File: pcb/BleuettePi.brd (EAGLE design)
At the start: 85 x 56 mm, 104 parts, among them IC1 PIC18F452, IC2 DS1339, IC3 MAX4173FESA+, IC5 MCP23017SS, IC6 LM386M-1, IC7 GY-27, Q1 10Mhz

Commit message: First Python code
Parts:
- removed D3: 5v1, diode:SOT23
- added D1: 5v1, diode:SOT23
- added D2: 3V3, diode:SOT23
- C1, C2: value (none) -> 470uf
- C12, C16, C6: value (none) -> 100nf
- C13: value (none) -> 4.7uf; device rcl:PANASONIC_A -> rcl:CT3528
- C14, C15: device rcl:PANASONIC_A -> rcl:CT3528
- C20: value (none) -> 10uf; device rcl:PANASONIC_A -> rcl:CT3528
- C9: value (none) -> 100uf
- IC2: value DS1339 -> DS1307
- Q6: value (none) -> 32.768KHz
- R19: value 10 -> 1k
- S0, S1, S10, S11, S2, S3, S4, S5, S6, S7, S8, S9, SX, SY: value (none) -> CONN_SERVO; device con-lstb:MA03-1 -> bleuette:CONN_SERVO
- moved C9 22.9 mm to (20.3, 5.40), turned to 270 degrees
- moved S0 13.7 mm to (33.7, 4.45), turned to 270 degrees
- moved S1 12.7 mm to (36.2, 4.45), turned to 270 degrees
- moved S2 11.7 mm to (38.7, 4.45), turned to 270 degrees
- moved S3 10.8 mm to (41.3, 4.45), turned to 270 degrees
- moved SX 10.4 mm to (26.0, 4.45), turned to 270 degrees
- moved S4 9.84 mm to (43.8, 4.45), turned to 270 degrees
- moved S5 8.89 mm to (46.4, 4.45), turned to 270 degrees
- moved SY 8.76 mm to (28.6, 4.45), turned to 270 degrees
- moved T_LVOLTAGE 3.88 mm to (21.0, 28.3)
- moved BATT 2.62 mm to (2.22, 39.5)
- moved BATT1 2.62 mm to (2.22, 37.0)
- moved ING 2.54 mm to (73.7, 3.17)
- moved INR 2.54 mm to (76.2, 3.17)
- moved S6 2.54 mm to (51.4, 4.45), turned to 270 degrees
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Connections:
- net +5V: now also SPLY.1; no longer SPLY.3
- net +7V: now also SPLY.3; no longer SPLY.1
- net AN6: now also D1.3; no longer D3.3
- net N$19: now also SX.S; no longer SX.3
- net N$24: now also SY.S; no longer SY.3
- net N$58: now also CR1220.+2; no longer CR1220.-
- net RX_PI: now also D2.3
- net SS0: now also S0.S; no longer S0.3
- net SS1: now also S1.S; no longer S1.3
- net SS10: now also S10.S; no longer S10.3
- net SS11: now also S11.S; no longer S11.3
- net SS2: now also S2.S; no longer S2.3
- net SS3: now also S3.S; no longer S3.3
- net SS4: now also S4.S; no longer S4.3
- net SS5: now also S5.S; no longer S5.3
- net SS6: now also S6.S; no longer S6.3
- net SS7: now also S7.S; no longer S7.3
- net SS8: now also S8.S; no longer S8.3
- net SS9: now also S9.S; no longer S9.3
- net VEE: now also S0.+, S1.+, S10.+, S11.+, S2.+, S3.+, S4.+, S5.+, S6.+, S7.+, S8.+, S9.+, SX.+, SY.+; no longer S0.2, S1.2, S10.2, S11.2, S2.2, S3.2, S4.2, S5.2, S6.2, S7.2, S8.2, S9.2, SX.2, SY.2
- net VSS: now also CR1220.-, D1.1, D2.1, S0.-, S1.-, S10.-, S11.-, S2.-, S3.-, S4.-, S5.-, S6.-, S7.-, S8.-, S9.-, SX.-, SY.-; no longer CR1220.+1, CR1220.+2, D3.1, S0.1, S1.1, S10.1, S11.1, S2.1, S3.1, S4.1, S5.1, S6.1, S7.1, S8.1, S9.1, SX.1, SY.1
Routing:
- net VSS: track 68.8 -> 114.1 mm, vias 9 -> 11
- net VEE: track 94.7 -> 68.3 mm, vias 1 -> 0
- net +5V: track 383.2 -> 363.8 mm
- net SS2: track 15.3 -> 5.64 mm
- net SS0: track 24.0 -> 15.1 mm
- net SS1: track 20.1 -> 13.8 mm
- net SS3: track 12.5 -> 6.36 mm
- net AN6: track 35.9 -> 41.6 mm
- net N$19: track 15.7 -> 20.9 mm
- net N$58: track 15.8 -> 12.3 mm
- net SS6: track 8.81 -> 11.9 mm
- net SS4: track 10.1 -> 7.08 mm
- net VDD: track 28.8 -> 31.6 mm
- net RX_PI: track 32.5 -> 35.2 mm
- net SS7: track 11.8 -> 13.9 mm
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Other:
- board text added: "Rev. 1.x.x"
- board text removed: "Rev. 1.0.0"

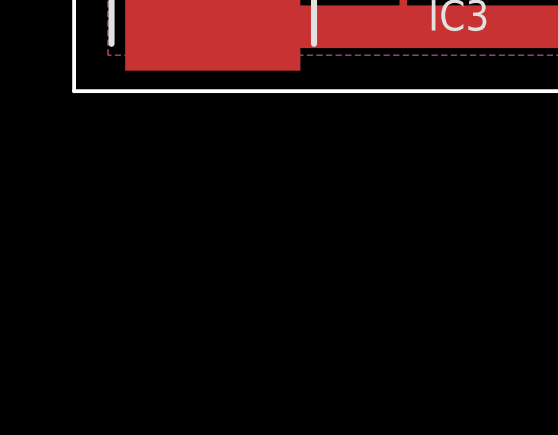
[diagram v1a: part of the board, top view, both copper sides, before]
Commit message: Added R4, MCLR pullup
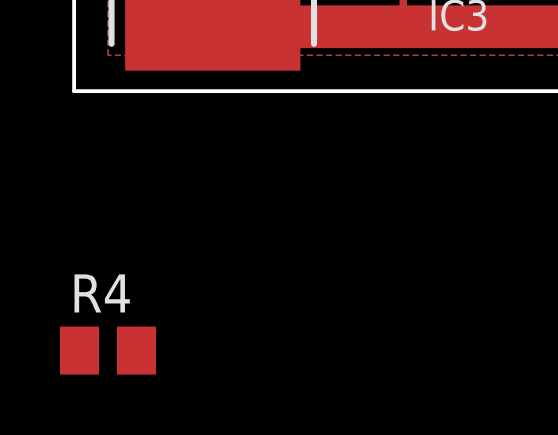
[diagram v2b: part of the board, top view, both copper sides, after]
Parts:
- added R4: 10k, rcl:M0805
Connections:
- net N$16 renamed TX_PIC
- net +5V: now also R4.2
- net UC_RESET: now also R4.1
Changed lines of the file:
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@@
 <attribute name="VALUE" x="49.2125" y="31.75" size="1.27" layer="27" rot="R90"/>
 </element>
+<element name="R4" library="rcl" package="M0805" value="10k" x="1.27" y="-8.5725"/>
 </elements>
 <signals>
@@
 <wire x1="45.95" y1="32.7025" x2="46.0375" y2="32.79" width="0.4064" layer="1"/>
 <wire x1="46.0375" y1="32.79" x2="46.0375" y2="30.1625" width="0.4064" layer="1"/>
+<contactref element="R4" pad="2"/>
 <wire x1="73.3425" y1="14.8925" x2="73.255" y2="14.9225" width="0" layer="19" extent="1-1"/>
+<wire x1="2.22" y1="-8.5725" x2="13.6525" y2="9.9187" width="0" layer="19" extent="1-1"/>
 </signal>
 <signal name="VDD">
@@
 <wire x1="51.1175" y1="13.0175" x2="45.085" y2="19.05" width="0.254" layer="16"/>
 <wire x1="45.085" y1="19.05" x2="45.085" y2="20.0025" width="0.254" layer="16"/>
+<contactref element="R4" pad="1"/>
+<wire x1="0.32" y1="-8.5725" x2="45.085" y2="19.05" width="0" layer="19" extent="1-16"/>
 </signal>
 <signal name="VEE">
@@
 <wire x1="24.13" y1="26.5225" x2="24.3" y2="26.3525" width="0.254" layer="1"/>
 </signal>
-<signal name="N$16">
+<signal name="TX_PIC">
 <contactref element="IC1" pad="44"/>
 <wire x1="36.11" y1="14.415" x2="32.8925" y2="14.415" width="0.254" layer="1"/>

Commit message: Dev Python BleuettePi
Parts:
- moved R4 57.0 mm to (53.7, 14.0)
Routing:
- net +5V: track 363.8 -> 368.7 mm, vias 7 -> 8
- net UC_RESET: track 12.4 -> 17.3 mm, vias 1 -> 2
- net VSS: vias 11 -> 10
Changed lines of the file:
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@@
 <element name="RST" library="testpad" package="TP20R" value="TPTP20R" x="51.1175" y="13.0175" smashed="yes" rot="MR90">
 <attribute name="TP_SIGNAL_NAME" value="" x="48.5775" y="13.0175" size="1" layer="38" rot="MR90"/>
-<attribute name="NAME" x="49.8" y="15.46" size="1.016" layer="26" rot="MR180"/>
+<attribute name="NAME" x="49.8" y="11.65" size="1.016" layer="26" rot="MR180"/>
 <attribute name="VALUE" x="50.1015" y="12.2555" size="0.0254" layer="28" rot="MR90"/>
 </element>
 <element name="VDD" library="testpad" package="TP20R" value="TPTP20R" x="48.5775" y="13.0175" smashed="yes" rot="MR90">
 <attribute name="TP_SIGNAL_NAME" value="" x="46.0375" y="13.0175" size="1" layer="38" rot="MR90"/>
-<attribute name="NAME" x="47.26" y="11.3325" size="1.016" layer="26" rot="MR180"/>
+<attribute name="NAME" x="46.9425" y="15.46" size="1.016" layer="26" rot="MR180"/>
 <attribute name="VALUE" x="47.5615" y="12.2555" size="0.0254" layer="28" rot="MR90"/>
 </element>
 <element name="VSS" library="testpad" package="TP20R" value="TPTP20R" x="46.0375" y="13.0175" smashed="yes" rot="MR90">
 <attribute name="TP_SIGNAL_NAME" value="" x="43.4975" y="13.0175" size="1" layer="38" rot="MR90"/>
-<attribute name="NAME" x="44.72" y="15.46" size="1.016" layer="26" rot="MR180"/>
+<attribute name="NAME" x="44.72" y="11.65" size="1.016" layer="26" rot="MR180"/>
 <attribute name="VALUE" x="45.0215" y="12.2555" size="0.0254" layer="28" rot="MR90"/>
 </element>
 <element name="PGD" library="testpad" package="TP20R" value="TPTP20R" x="43.4975" y="13.0175" smashed="yes" rot="MR90">
 <attribute name="TP_SIGNAL_NAME" value="" x="40.9575" y="13.0175" size="1" layer="38" rot="MR90"/>
-<attribute name="NAME" x="41.8625" y="11.3325" size="1.016" layer="26" rot="MR180"/>
+<attribute name="NAME" x="41.8625" y="15.46" size="1.016" layer="26" rot="MR180"/>
 <attribute name="VALUE" x="42.4815" y="12.2555" size="0.0254" layer="28" rot="MR90"/>
 </element>
 <element name="PGC" library="testpad" package="TP20R" value="TPTP20R" x="40.9575" y="13.0175" smashed="yes" rot="MR90">
 <attribute name="TP_SIGNAL_NAME" value="" x="38.4175" y="13.0175" size="1" layer="38" rot="MR90"/>
-<attribute name="NAME" x="39.3225" y="15.46" size="1.016" layer="26" rot="MR180"/>
+<attribute name="NAME" x="39.3225" y="11.65" size="1.016" layer="26" rot="MR180"/>
 <attribute name="VALUE" x="39.9415" y="12.2555" size="0.0254" layer="28" rot="MR90"/>
 </element>
@@
 <attribute name="VALUE" x="49.2125" y="31.75" size="1.27" layer="27" rot="R90"/>
 </element>
-<element name="R4" library="rcl" package="M0805" value="10k" x="1.27" y="-8.5725"/>
+<element name="R4" library="rcl" package="M0805" value="10k" x="53.6575" y="13.97" smashed="yes">
+<attribute name="NAME" x="52.07" y="14.9225" size="1.016" layer="25"/>
+<attribute name="VALUE" x="52.3875" y="11.43" size="1.27" layer="27"/>
+</element>
 </elements>
 <signals>
@@
 <contactref element="C16" pad="2"/>
 <contactref element="R15" pad="1"/>
-<via x="56.8325" y="12.7" extent="1-16" drill="0.6" diameter="1.4224"/>
 <contactref element="C6" pad="1"/>
 <contactref element="IC2" pad="4"/>
@@
 <wire x1="66.04" y1="10.16" x2="61.75375" y2="10.16" width="0.4064" layer="16"/>
 <wire x1="61.75375" y1="10.16" x2="61.43625" y2="10.4775" width="0.4064" layer="16"/>
-<wire x1="61.43625" y1="10.4775" x2="48.5775" y2="10.4775" width="0.4064" layer="16"/>
+<wire x1="61.43625" y1="10.4775" x2="56.1975" y2="10.4775" width="0.4064" layer="16"/>
 <via x="35.56" y="10.4775" extent="1-16" drill="0.6" diameter="1.4224"/>
+<wire x1="56.1975" y1="10.4775" x2="48.5775" y2="10.4775" width="0.4064" layer="16"/>
 <wire x1="48.5775" y1="10.4775" x2="35.56" y2="10.4775" width="0.4064" layer="16"/>
 <wire x1="18.415" y1="10.4775" x2="35.56" y2="10.4775" width="0.4064" layer="1"/>
@@
 <wire x1="46.0375" y1="32.79" x2="46.0375" y2="30.1625" width="0.4064" layer="1"/>
 <contactref element="R4" pad="2"/>
+<wire x1="54.6075" y1="13.97" x2="55.88" y2="13.97" width="0.254" layer="1"/>
+<wire x1="55.88" y1="13.97" x2="56.1975" y2="13.6525" width="0.254" layer="1"/>
+<wire x1="56.1975" y1="13.6525" x2="56.1975" y2="12.7" width="0.254" layer="1"/>
+<wire x1="56.1975" y1="12.7" x2="56.1975" y2="10.4775" width="0.254" layer="16"/>
+<via x="56.1975" y="12.7" extent="1-16" drill="0.6" diameter="1.4224"/>
 <wire x1="73.3425" y1="14.8925" x2="73.255" y2="14.9225" width="0" layer="19" extent="1-1"/>
-<wire x1="2.22" y1="-8.5725" x2="13.6525" y2="9.9187" width="0" layer="19" extent="1-1"/>
 </signal>
 <signal name="VDD">
@@
 <wire x1="45.085" y1="19.05" x2="45.085" y2="20.0025" width="0.254" layer="16"/>
 <contactref element="R4" pad="1"/>
-<wire x1="0.32" y1="-8.5725" x2="45.085" y2="19.05" width="0" layer="19" extent="1-16"/>
+<wire x1="51.1175" y1="13.0175" x2="51.1175" y2="15.24" width="0.254" layer="16"/>
+<via x="51.1175" y="15.24" extent="1-16" drill="0.6" diameter="1.4224"/>
+<wire x1="51.1175" y1="15.24" x2="51.1175" y2="14.2875" width="0.254" layer="1"/>
+<wire x1="51.1175" y1="14.2875" x2="51.435" y2="13.97" width="0.254" layer="1"/>
+<wire x1="51.435" y1="13.97" x2="52.7075" y2="13.97" width="0.254" layer="1"/>
 </signal>
 <signal name="VEE">

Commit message: Modif PCB
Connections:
- net N$1 renamed RC1
- net N$2 renamed RC2
- net N$3 renamed RC3
- net N$55 renamed RC4
- net N$56 renamed RC5
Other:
- board text added: "Remonter GY-27"
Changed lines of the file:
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@@
 <wire x1="27.94" y1="36.83" x2="28.575" y2="36.195" width="0.3048" layer="21"/>
 <wire x1="20.47875" y1="19.3675" x2="20.955" y2="21.11375" width="0.127" layer="21"/>
+<text x="40.3225" y="57.4675" size="1.6764" layer="19">Remonter GY-27</text>
 </plain>
 <attributes>
@@
 <wire x1="74.6125" y1="10.4775" x2="73.975" y2="10.4775" width="0.254" layer="1"/>
 </signal>
-<signal name="N$55">
+<signal name="RC4">
 <contactref element="IC1" pad="42"/>
 <contactref element="RC4" pad="TP"/>
@@
 <wire x1="34.785" y1="16.015" x2="34.76625" y2="16.03375" width="0.254" layer="1"/>
 </signal>
-<signal name="N$56">
+<signal name="RC5">
 <contactref element="IC1" pad="43"/>
 <contactref element="RC5" pad="TP"/>
@@
 <wire x1="53.975" y1="26.035" x2="53.975" y2="31.115" width="0.254" layer="16"/>
 </signal>
-<signal name="N$1">
+<signal name="RC1">
 <contactref element="IC1" pad="35"/>
 <contactref element="RC1" pad="TP"/>
@@
 <wire x1="34.79125" y1="21.615" x2="34.76625" y2="21.59" width="0.254" layer="1"/>
 </signal>
-<signal name="N$2">
+<signal name="RC2">
 <contactref element="IC1" pad="36"/>
 <contactref element="RC2" pad="TP"/>
@@
 <wire x1="34.785" y1="20.815" x2="34.76625" y2="20.79625" width="0.254" layer="1"/>
 </signal>
-<signal name="N$3">
+<signal name="RC3">
 <contactref element="IC1" pad="37"/>
 <contactref element="RC3" pad="TP"/>

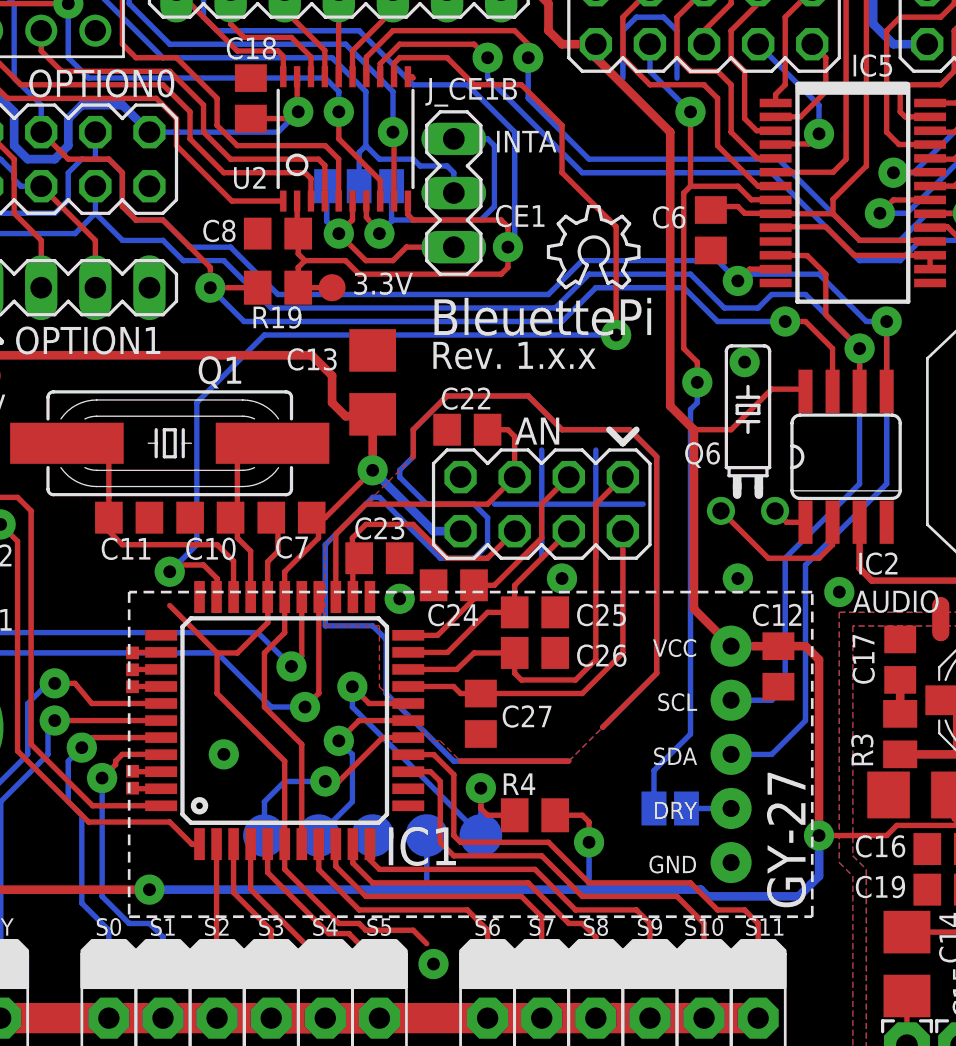
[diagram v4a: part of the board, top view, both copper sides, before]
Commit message: PCB: GY-27 remonté
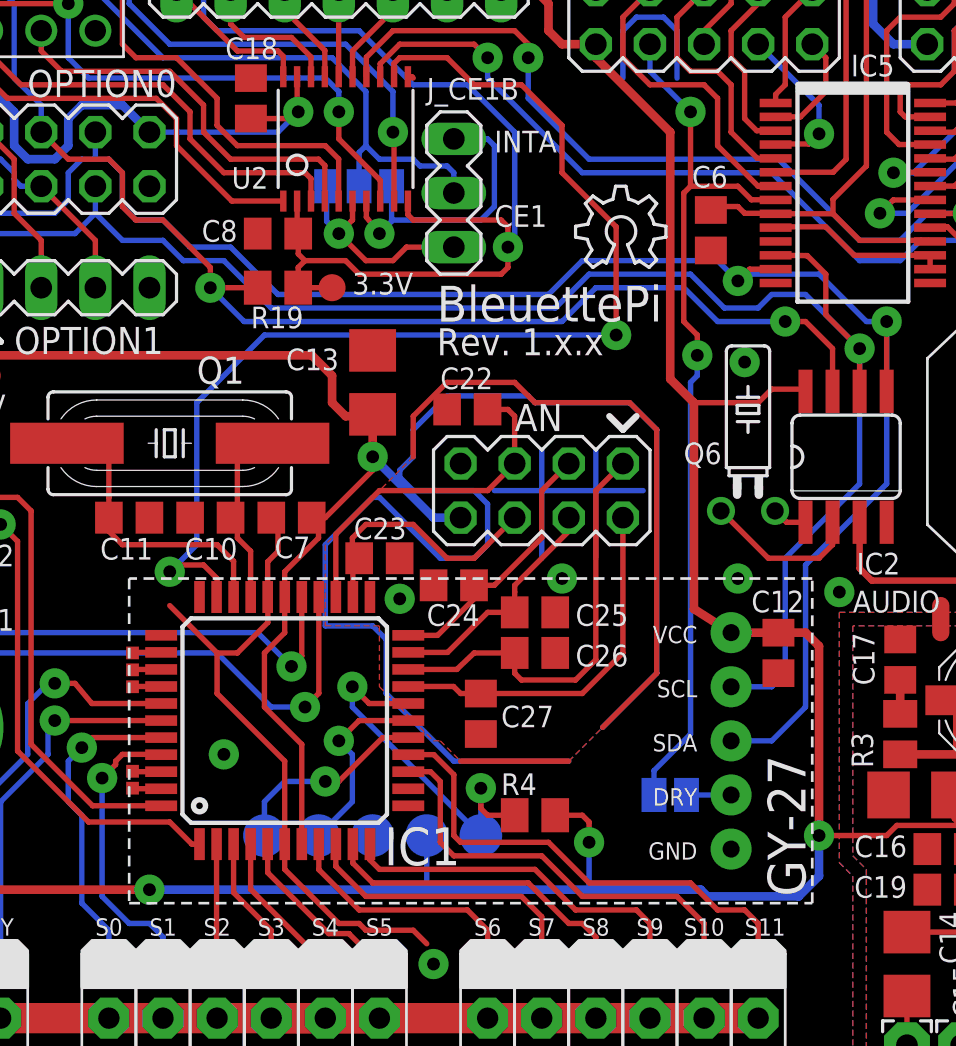
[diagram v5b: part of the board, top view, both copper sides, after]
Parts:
- moved U$5 1.59 mm to (55.6, 39.7)
- moved C22 0.95 mm to (50.5, 33.0)
- moved AN 0.64 mm to (54.0, 29.2)
- moved C12 0.64 mm to (65.1, 21.6)
- moved DRDY 0.63 mm to (60.0, 14.9)
- moved IC7 0.63 mm to (66.7, 25.1)
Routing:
- net AGND: track 115.6 -> 118.3 mm
- net +5V: track 368.7 -> 367.9 mm
- net GPB7: track 42.2 -> 41.5 mm
- net AN3: track 12.2 -> 12.9 mm
- net AN2: track 10.6 -> 11.3 mm
- net AN1: track 19.7 -> 20.3 mm
- net AN0: track 16.1 -> 16.7 mm
- net SDA: track 87.3 -> 86.7 mm
- net SCL: track 84.7 -> 84.1 mm
- net AN5: track 15.8 -> 16.3 mm

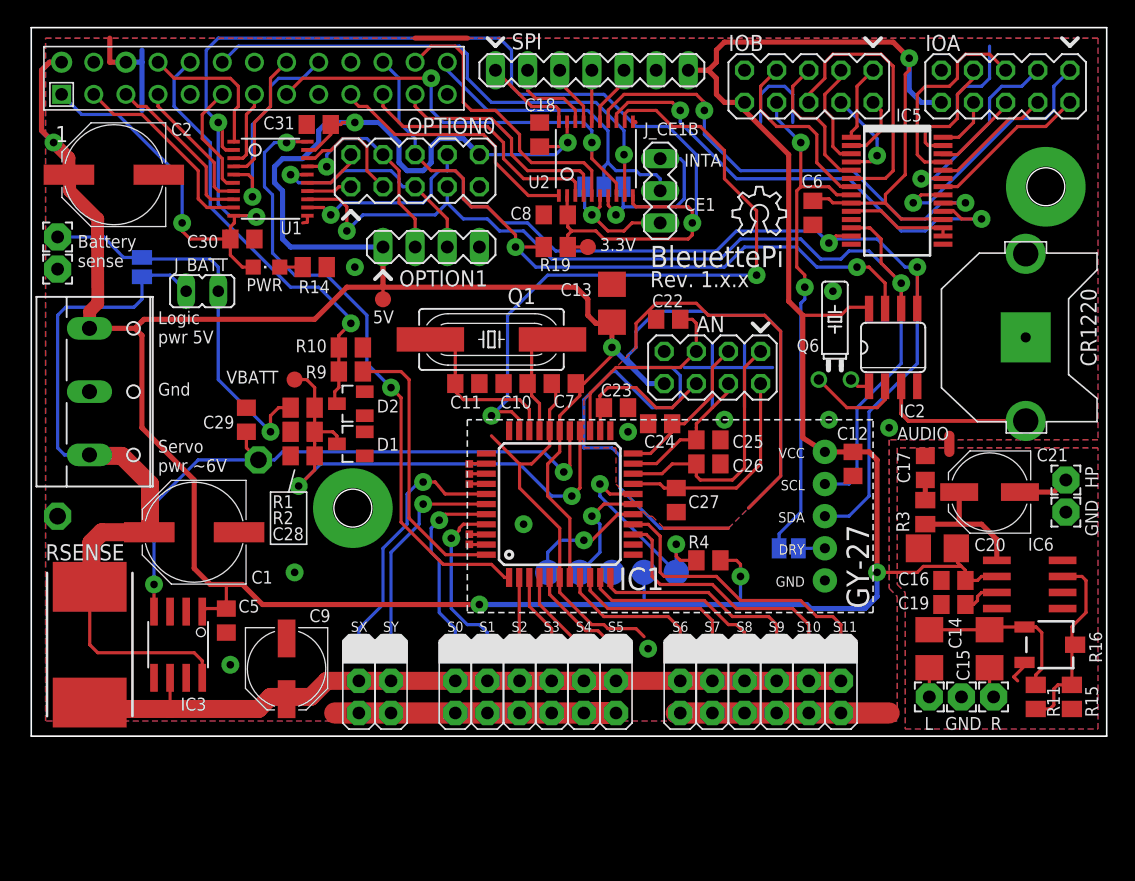
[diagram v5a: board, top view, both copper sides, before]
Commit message: PCB: Inverse location of batt sense and power connector
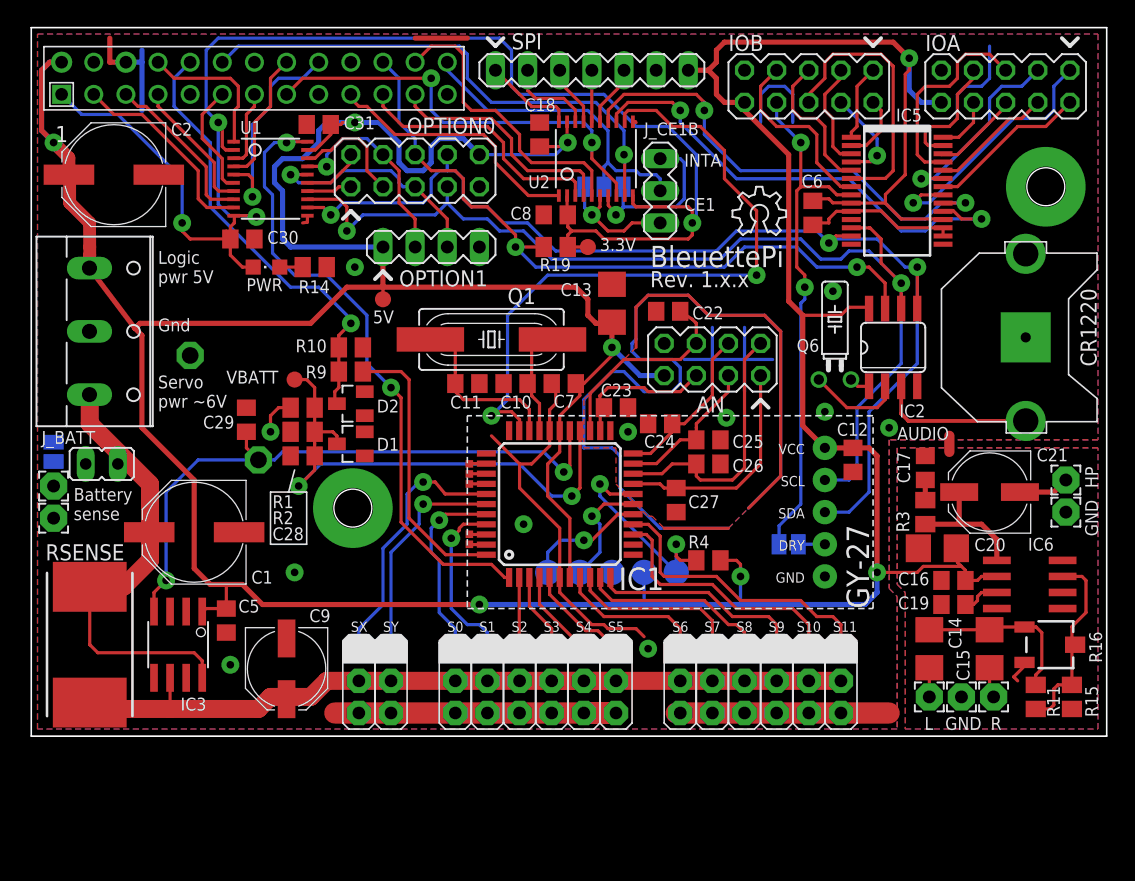
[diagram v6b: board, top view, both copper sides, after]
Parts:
- moved BATT 19.7 mm to (1.91, 19.8)
- moved BATT1 19.7 mm to (1.91, 17.3)
- moved TP1 16.5 mm to (12.7, 30.2)
- moved J_BATT0 16.2 mm to (1.91, 22.5), turned to 270 degrees
- moved J_BATT1 15.8 mm to (5.71, 21.6)
- moved SPLY 4.76 mm to (6.03, 32.1)
- moved AN 0.63 mm to (54.0, 29.8)
- moved C22 0.63 mm to (50.5, 33.7)
- moved DRDY 0.32 mm to (60.0, 15.2)
- moved C12 0.32 mm to (65.1, 21.9)
- moved IC7 0.32 mm to (66.7, 25.4)
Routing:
- net VDD: track 31.6 -> 3.12 mm
- net +7V: track 60.1 -> 36.9 mm
- net VSS: track 114.1 -> 117.7 mm
- net +5V: track 367.9 -> 364.4 mm
- net AGND: track 118.3 -> 119.5 mm
- net AN4: track 11.9 -> 11.1 mm
- net AN3: track 12.9 -> 13.5 mm
- net AN2: track 11.3 -> 11.9 mm
- net AN1: track 20.3 -> 21.0 mm
- net AN0: track 16.7 -> 17.4 mm
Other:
- board text removed: "Remonter GY-27"
